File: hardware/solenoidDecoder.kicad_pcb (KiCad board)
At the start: 2 copper layers, 54.5 x 73 mm, 134 parts, among them J3 ICSP, J62 Screw_Terminal_01x04, Q11 AO3400A, Q12 AO3400A, Q21 AO3400A, Q22 AO3400A, Q31 AO3400A, Q32 AO3400A, Q41 AO3400A, Q42 AO3400A, Q51 AO3400A, Q52 AO3400A, Q61 AO3400A, Q62 AO3400A, Q71 AO3400A, Q72 AO3400A, Q81 AO3400A, Q82 AO3400A, SW1 SW_SPST, U1 ATmega328-A, U3 6N137, U301 AMS1117-5.0, Y1 Crystal_GND2

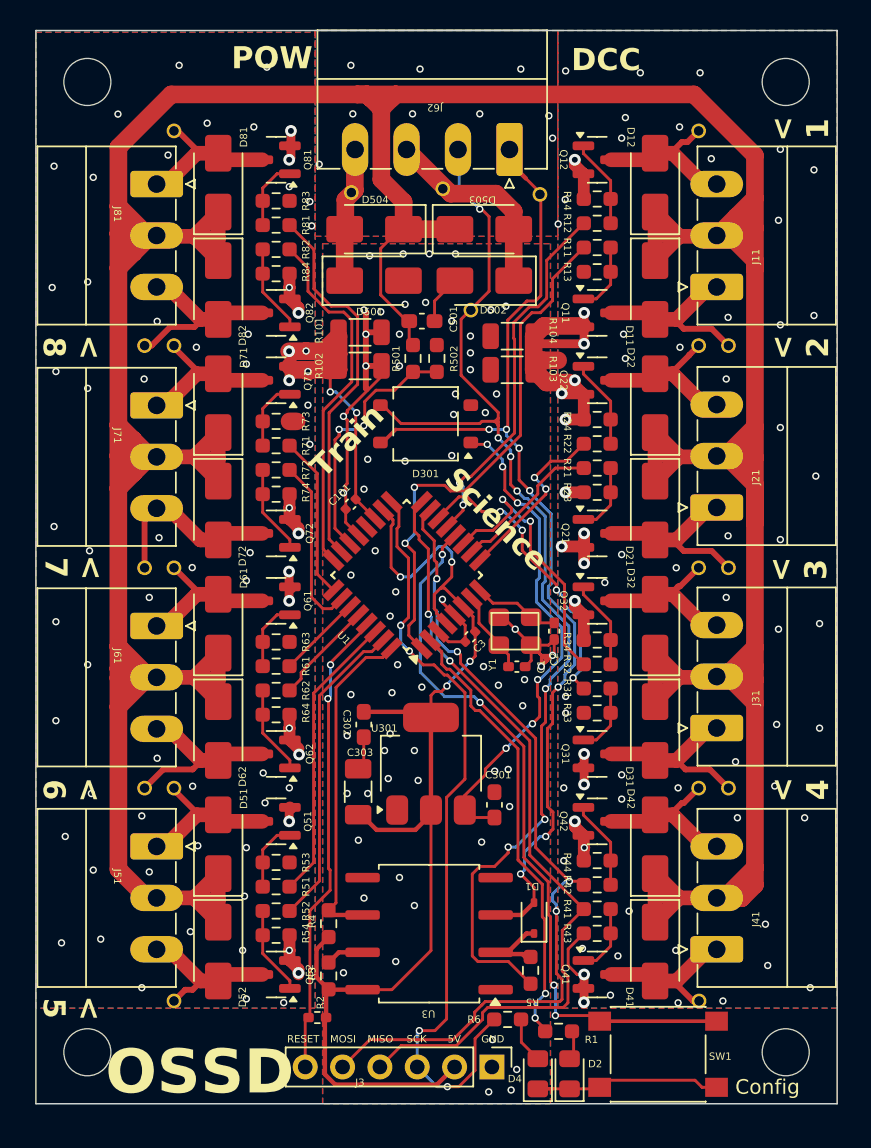
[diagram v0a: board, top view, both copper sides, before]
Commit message: organized board files and added pictures
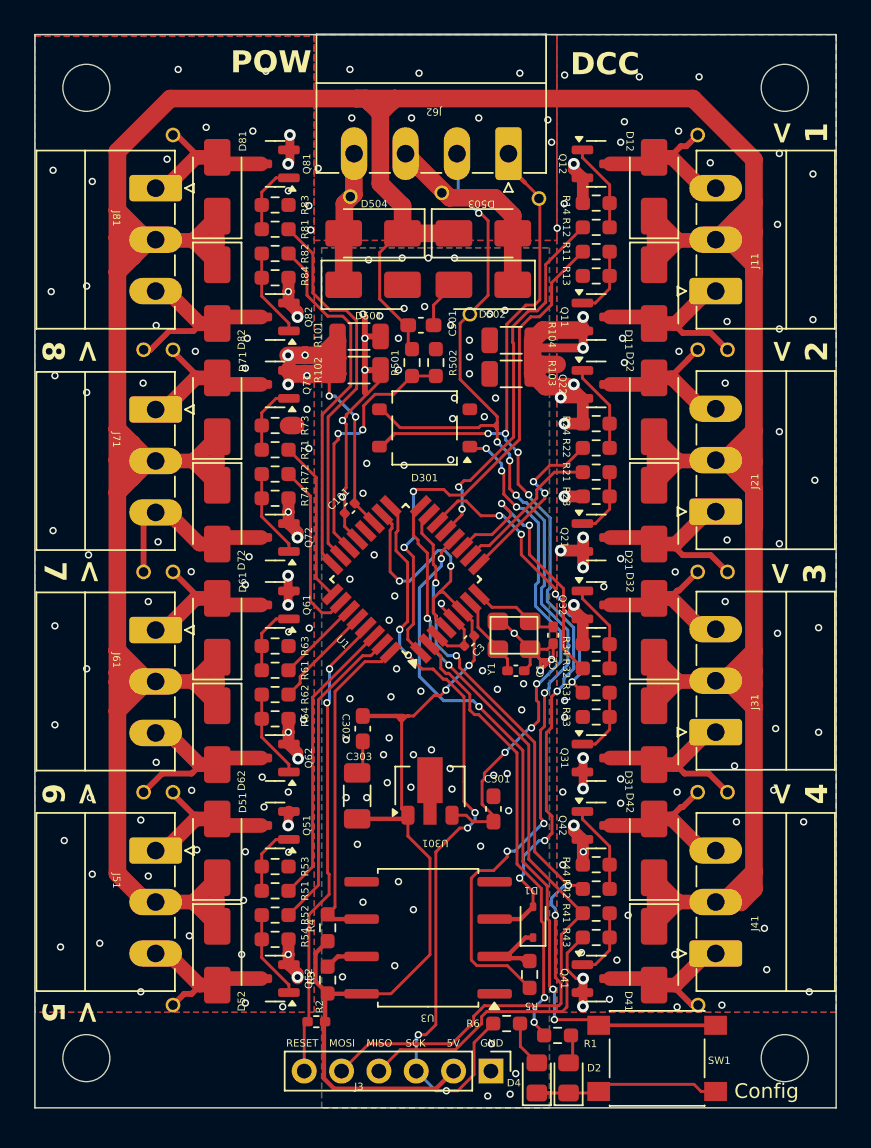
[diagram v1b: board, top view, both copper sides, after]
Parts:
- removed the G*** at (131.1, 93.6)
- removed the G*** at (130.8, 125.1)
- removed the REF** at (106.1, 66.1)
- removed the REF** at (106.1, 132.1)
- removed the REF** at (153.6, 132.1)
- removed the REF** at (153.6, 66.1)
- removed the REF** at (130.8, 108.5)
- added G***: LOGO, custom_kicad_lib_sk:OS-model-railway-electronics, B.Cu at (129.4, 106.8)
- added REF**: MountingHole_3.2mm_M3, MountingHole:MountingHole_3.2mm_M3, F.Cu at (153.5, 66.5)
- added REF**: MountingHole_3.2mm_M3, MountingHole:MountingHole_3.2mm_M3, F.Cu at (153.5, 132.5)
- added REF**: MountingHole_3.2mm_M3, MountingHole:MountingHole_3.2mm_M3, F.Cu at (106.0, 66.5)
- added REF**: MountingHole_3.2mm_M3, MountingHole:MountingHole_3.2mm_M3, F.Cu at (106.0, 132.5)
- U301: value AMS1117-5.0 -> L78L05_SOT89; footprint Package_TO_SOT_SMD:SOT-223-3_TabPin2 -> Package_TO_SOT_SMD:SOT-89-3
- moved U301 1.55 mm to (129.4, 114.0)
- moved C3 0.29 mm to (132.0, 104.1)
- moved C501 0.29 mm to (128.8, 82.6)
- moved R5 0.29 mm to (136.1, 126.8)
- moved TP1 0.29 mm to (149.6, 99.4)
- moved TP3 0.29 mm to (149.6, 84.3)
- moved TP7 0.29 mm to (147.6, 128.9)
- moved Y1 0.29 mm to (135.1, 103.7)
- moved C302 0.29 mm to (124.8, 110.1)
- moved C303 0.29 mm to (124.4, 114.7)
- moved J51 0.29 mm to (110.7, 118.4)
- moved J61 0.29 mm to (110.7, 103.4)
- moved J71 0.29 mm to (110.7, 88.4)
- moved Q51 0.29 mm to (118.8, 116.7)
- moved Q61 0.29 mm to (118.8, 101.7)
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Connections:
- U301 pad 1: GND -> +5V
- U301 pad 2: +5V -> GND
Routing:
- net Net-(D301-+): track 32.9 -> 34.7 mm
- net /uController/LED: track 52.0 -> 52.6 mm, vias 4 -> 6
- net GND_COIL: vias 149 -> 152
- net GND: vias 66 -> 69
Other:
- board text removed: "Manual"
- board text removed: "OSSD"
- board text removed: "Science"
- board text removed: "Train"
